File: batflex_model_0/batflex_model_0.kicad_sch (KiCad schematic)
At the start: 12 parts, among them J1 molex_505004, J2 molex_505006

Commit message: Add footprints to resistors...
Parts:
- R1, R2, R3, R4: footprint (none) -> Resistor_SMD:R_0402_1005Metric
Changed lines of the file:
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@@
   (junction (at 157.48 49.53) (diameter 1.016) (color 0 0 0 0))
   (junction (at 162.56 45.72) (diameter 1.016) (color 0 0 0 0))
-  (bus_entry (at 101.6 19.05) (size 2.54 2.54)
-    (stroke (width 0.1524) (type solid) (color 0 0 0 0))
-  )
   (wire (pts (xy 74.93 49.53) (xy 143.51 49.53))
     (stroke (width 0) (type solid) (color 0 0 0 0))
@@
       (effects (font (size 1.27 1.27)) (justify left))
     )
-    (property "Footprint" "" (id 2) (at 73.152 59.69 90)
+    (property "Footprint" "Resistor_SMD:R_0402_1005Metric" (id 2) (at 73.152 59.69 90)
       (effects (font (size 1.27 1.27)) hide)
     )
@@
       (effects (font (size 1.27 1.27)) (justify left))
     )
-    (property "Footprint" "" (id 2) (at 84.582 59.69 90)
+    (property "Footprint" "Resistor_SMD:R_0402_1005Metric" (id 2) (at 84.582 59.69 90)
       (effects (font (size 1.27 1.27)) hide)
     )
@@
       (effects (font (size 1.27 1.27)) (justify left))
     )
-    (property "Footprint" "" (id 2) (at 118.872 59.69 90)
+    (property "Footprint" "Resistor_SMD:R_0402_1005Metric" (id 2) (at 118.872 59.69 90)
       (effects (font (size 1.27 1.27)) hide)
     )
@@
       (effects (font (size 1.27 1.27)) (justify left))
     )
-    (property "Footprint" "" (id 2) (at 130.302 59.69 90)
+    (property "Footprint" "Resistor_SMD:R_0402_1005Metric" (id 2) (at 130.302 59.69 90)
       (effects (font (size 1.27 1.27)) hide)
     )
@@
     )
     (path "/fb77e734-b0cc-4eac-a662-ba301895c38b"
-      (reference "R1") (unit 1) (value "1K") (footprint "")
+      (reference "R1") (unit 1) (value "1K") (footprint "Resistor_SMD:R_0402_1005Metric")
     )
     (path "/a5d9d177-1824-4706-99be-1da0836b2a29"
-      (reference "R2") (unit 1) (value "1K") (footprint "")
+      (reference "R2") (unit 1) (value "1K") (footprint "Resistor_SMD:R_0402_1005Metric")
     )
     (path "/f130de7a-f243-44b0-94cf-81fd8569087a"
-      (reference "R3") (unit 1) (value "1K") (footprint "")
+      (reference "R3") (unit 1) (value "1K") (footprint "Resistor_SMD:R_0402_1005Metric")
     )
     (path "/c2ed16f9-14d2-4850-851c-ded21e8fb428"
-      (reference "R4") (unit 1) (value "1K") (footprint "")
+      (reference "R4") (unit 1) (value "1K") (footprint "Resistor_SMD:R_0402_1005Metric")
     )
     (path "/1f682d86-9d69-45ee-a128-66fd8a1f678e"

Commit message: Add protection and fix duck
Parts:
- added D101, D102, D103, D104, D105, D106: MM5Zxx, Diode_SMD:D_SOD-523, symbol Diode:MM5Zxx
- renumbered TP01 to TP1, TP02 to TP2, TP03 to TP3
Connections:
- net GND: now reaches J1.7 (Pin_7), J1.8 (Pin_8), J2.1 (Pin_1), J2.2 (Pin_2), R2.1, R3.1, TP1.1, TP10.1
- net GND: now also D101.2 (A), D102.2 (A), D103.2 (A), D104.2 (A), D105.2 (A), D106.2 (A)
- net at J2.7 (Pin_7), J2.8 (Pin_8), R1.1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: now also D102.1 (K), D104.1 (K), D106.1 (K)
- net at J1.1 (Pin_1), J1.2 (Pin_2), R4.1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: now also D101.1 (K), D103.1 (K), D105.1 (K)
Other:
- note added: "Over voltage protection/clamps"

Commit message: Add random version string and date
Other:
- title: (none) -> The Ugly Duck
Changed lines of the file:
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@@
   (page 1 1)
   (paper "A4")
+  (title_block
+    (title "The Ugly Duck")
+    (date "2020-11-04")
+    (rev "v1")
+  )
   (junction (at 52.07 66.04) (diameter 1.016) (color 0 0 0 0))
   (junction (at 52.07 73.66) (diameter 1.016) (color 0 0 0 0))

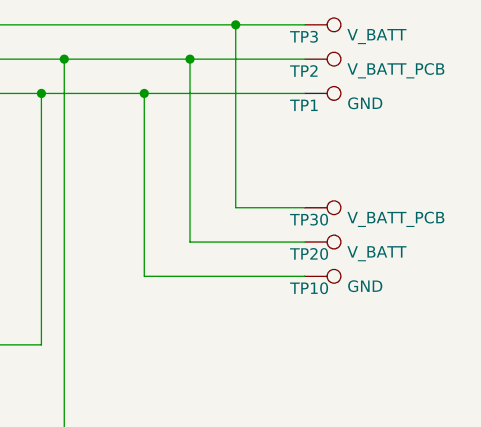
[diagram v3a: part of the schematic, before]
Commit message: Final PCB for batflex model 0 aka the ugly duck
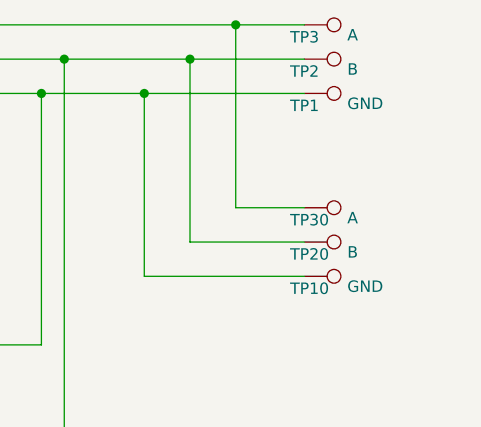
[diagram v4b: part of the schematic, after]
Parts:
- TP2: value V_BATT_PCB -> B
- TP20: value V_BATT -> B
- TP3: value V_BATT -> A
- TP30: value V_BATT_PCB -> A
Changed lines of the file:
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@@
       (effects (font (size 1.27 1.27)) (justify left))
     )
-    (property "Value" "V_BATT" (id 1) (at 174.9552 46.863 90)
+    (property "Value" "A" (id 1) (at 174.9552 46.863 90)
       (effects (font (size 1.27 1.27)) (justify left))
     )
@@
       (effects (font (size 1.27 1.27)) (justify left))
     )
-    (property "Value" "V_BATT_PCB" (id 1) (at 174.9552 50.673 90)
+    (property "Value" "B" (id 1) (at 174.9552 50.673 90)
       (effects (font (size 1.27 1.27)) (justify left))
     )
@@
       (effects (font (size 1.27 1.27)) (justify left))
     )
-    (property "Value" "V_BATT_PCB" (id 1) (at 174.9552 67.183 90)
+    (property "Value" "A" (id 1) (at 174.9552 67.183 90)
       (effects (font (size 1.27 1.27)) (justify left))
     )
@@
       (effects (font (size 1.27 1.27)) (justify left))
     )
-    (property "Value" "V_BATT" (id 1) (at 174.9552 70.993 90)
+    (property "Value" "B" (id 1) (at 174.9552 70.993 90)
       (effects (font (size 1.27 1.27)) (justify left))
     )
@@
     )
     (path "/392ee07e-677f-42fb-b7ba-f22a392de1ce"
-      (reference "TP2") (unit 1) (value "V_BATT_PCB") (footprint "batflex:wire_pad_2x4mm")
+      (reference "TP2") (unit 1) (value "B") (footprint "batflex:wire_pad_2x4mm")
     )
     (path "/117d0c5c-b3d2-4a82-872c-3a8a3be53c83"
-      (reference "TP3") (unit 1) (value "V_BATT") (footprint "batflex:wire_pad_2x4mm")
+      (reference "TP3") (unit 1) (value "A") (footprint "batflex:wire_pad_2x4mm")
     )
     (path "/cefe2c1e-c010-43b1-bf09-ea8c8bde63e4"
@@
     )
     (path "/66b6051a-5449-40bc-988a-d04c32b3a6e3"
-      (reference "TP20") (unit 1) (value "V_BATT") (footprint "batflex:wire_pad_2x4mm")
+      (reference "TP20") (unit 1) (value "B") (footprint "batflex:wire_pad_2x4mm")
     )
     (path "/3a28cfcf-7ecb-4298-b8de-fb538cfee930"
-      (reference "TP30") (unit 1) (value "V_BATT_PCB") (footprint "batflex:wire_pad_2x4mm")
-    )
-  )
+      (reference "TP30") (unit 1) (value "A") (footprint "batflex:wire_pad_2x4mm")
+    )
+  )
